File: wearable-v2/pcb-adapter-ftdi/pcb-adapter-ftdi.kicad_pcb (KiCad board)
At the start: 2 copper layers, 27.8 x 19.9 mm, 2 parts, among them J1 FTDI_HERALD, J2 FTDI Pins

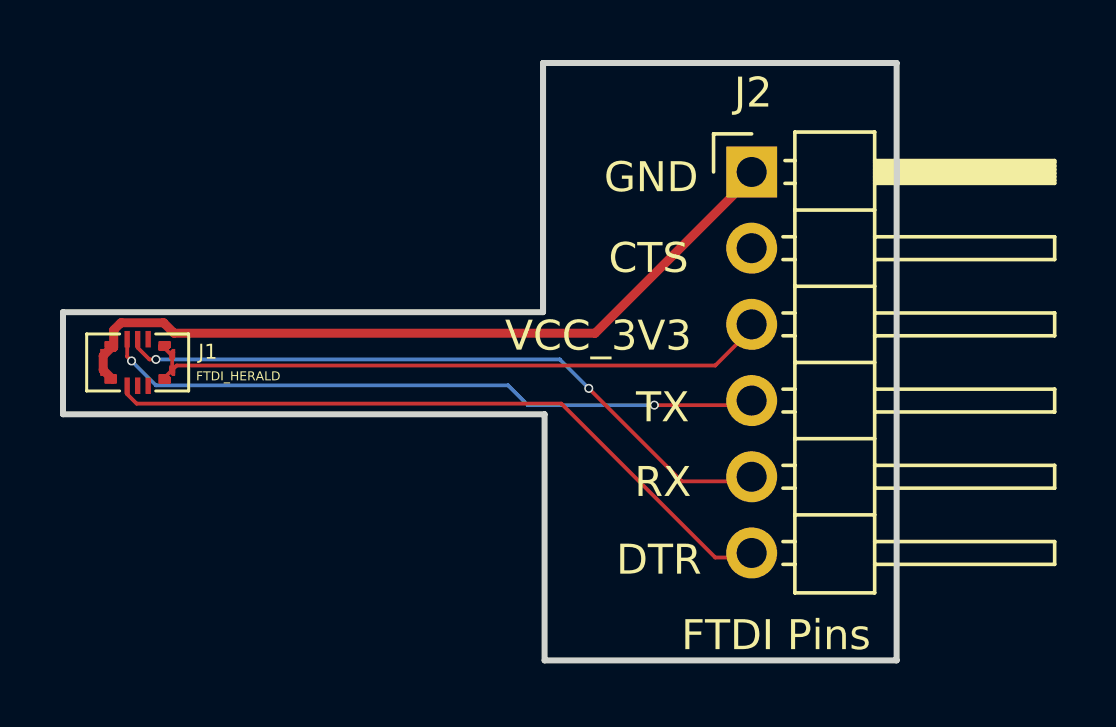
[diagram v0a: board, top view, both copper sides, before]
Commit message: Reworked boards for JLCPCB manufacture
Slightly larger Vias.
Added debug pin holes for Beta testing.
Signed-off-by: Adam Fowler <adam@adamfowler.org>
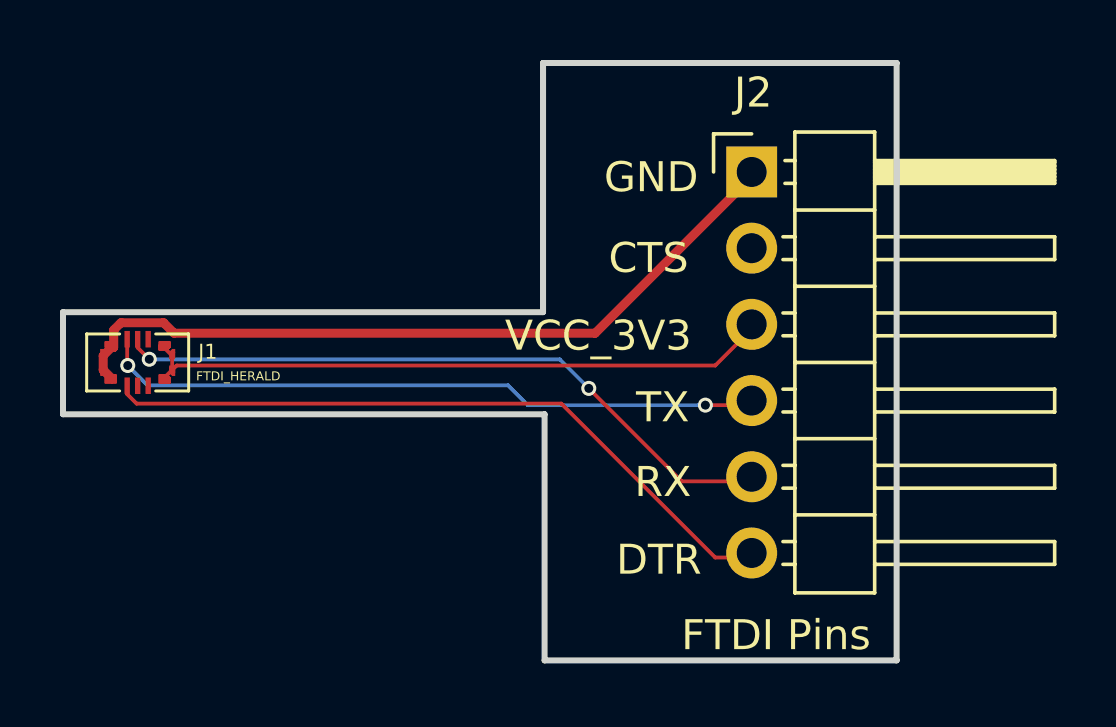
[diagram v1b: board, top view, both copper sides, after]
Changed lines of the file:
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@@
 (kicad_pcb (version 20221018) (generator pcbnew)
   (general
-    (thickness 1.2)
+    (thickness 1.6)
   )
   (paper "A4")
@@
       (layer "F.Mask" (type "Top Solder Mask") (thickness 0.01))
       (layer "F.Cu" (type "copper") (thickness 0.035))
-      (layer "dielectric 1" (type "core") (thickness 1.11) (material "FR4") (epsilon_r 4.5) (loss_tangent 0.02))
+      (layer "dielectric 1" (type "core") (thickness 1.51) (material "FR4") (epsilon_r 4.5) (loss_tangent 0.02))
       (layer "B.Cu" (type "copper") (thickness 0.035))
       (layer "B.Mask" (type "Bottom Solder Mask") (thickness 0.01))
@@
       (svgprecision 4)
       (plotframeref false)
-      (viasonmask false)
+      (viasonmask true)
       (mode 1)
       (useauxorigin true)
@@
         (effects (font (size 0.3 0.3) (thickness 0.075)))
     )
-    (fp_text user "${REFERENCE}" (at 0 0 unlocked) (layer "F.Fab")
+    (fp_text user "${REFERENCE}" (at 2.3622 1.0922 unlocked) (layer "F.Fab")
         (effects (font (size 0.3 0.3) (thickness 0.075)))
     )
@@
         (effects (font (size 1 1) (thickness 0.15)))
     )
-    (fp_text user "${REFERENCE}" (at 2.77 6.35 90) (layer "F.Fab")
+    (fp_text user "${REFERENCE}" (at 2.77 -2.667 180) (layer "F.Fab")
         (effects (font (size 1 1) (thickness 0.15)))
     )
@@
     )
     (stroke (width 0.2) (type solid)) (fill none) (layer "Edge.Cuts"))
-  (gr_text "The Herald Project\nHerald Micro FTDI to 6-pin out\nV1.0 Nov 2023\nLicense: CERN-OHL-P-2" (at 127.8636 84.836 90) (layer "B.SilkS")
+  (gr_text "The Herald Project\nHerald Micro FTDI to 6-pin out\nV1.0 Nov 2023\nLicense: CERN-OHL-P-2" (at 127.9144 84.328 90) (layer "B.SilkS")
     (effects (font (size 0.6 0.6) (thickness 0.15) bold) (justify left bottom mirror))
   )
@@
   (segment (start 125.0286 91.6334) (end 110.99271 91.6334) (width 0.3) (layer "F.Cu") (net 6))
   (segment (start 110.64271 91.2834) (end 109.22489 91.2834) (width 0.3) (layer "F.Cu") (net 6))
-  (segment (start 130.2512 94.0308) (end 127 94.0308) (width 0.127) (layer "F.Cu") (net 7))
-  (segment (start 109.4288 92.4108) (end 109.4288 91.8334) (width 0.127) (layer "F.Cu") (net 7))
-  (segment (start 109.5756 92.5576) (end 109.4288 92.4108) (width 0.127) (layer "F.Cu") (net 7))
-  (via (at 109.5756 92.5576) (size 0.3) (drill 0.2) (layers "F.Cu" "B.Cu") (net 7))
-  (via (at 127 94.0308) (size 0.3) (drill 0.2) (layers "F.Cu" "B.Cu") (net 7))
-  (segment (start 122.1232 93.3704) (end 122.7836 94.0308) (width 0.127) (layer "B.Cu") (net 7))
-  (segment (start 109.5756 92.5576) (end 110.3884 93.3704) (width 0.127) (layer "B.Cu") (net 7))
-  (segment (start 110.3884 93.3704) (end 122.1232 93.3704) (width 0.127) (layer "B.Cu") (net 7))
-  (segment (start 122.7836 94.0308) (end 127 94.0308) (width 0.127) (layer "B.Cu") (net 7))
+  (segment (start 109.4486 92.71) (end 109.4288 92.6902) (width 0.127) (layer "F.Cu") (net 7))
+  (segment (start 130.2512 94.0308) (end 128.7018 94.0308) (width 0.127) (layer "F.Cu") (net 7))
+  (segment (start 109.4288 92.6902) (end 109.4288 91.8334) (width 0.127) (layer "F.Cu") (net 7))
+  (via (at 109.4486 92.71) (size 0.5) (drill 0.3) (layers "F.Cu" "B.Cu") (net 7))
+  (via (at 128.7018 94.0308) (size 0.5) (drill 0.3) (layers "F.Cu" "B.Cu") (net 7))
+  (segment (start 122.7836 94.0308) (end 122.1232 93.3704) (width 0.127) (layer "B.Cu") (net 7))
+  (segment (start 122.1232 93.3704) (end 110.109 93.3704) (width 0.127) (layer "B.Cu") (net 7))
+  (segment (start 128.7018 94.0308) (end 122.7836 94.0308) (width 0.127) (layer "B.Cu") (net 7))
+  (segment (start 110.109 93.3704) (end 109.4486 92.71) (width 0.127) (layer "B.Cu") (net 7))
   (segment (start 109.4288 93.66498) (end 109.4288 93.3834) (width 0.127) (layer "F.Cu") (net 8))
   (segment (start 109.74382 93.98) (end 109.4288 93.66498) (width 0.127) (layer "F.Cu") (net 8))
@@
   (segment (start 123.9012 93.98) (end 109.74382 93.98) (width 0.127) (layer "F.Cu") (net 8))
   (segment (start 130.2512 99.1108) (end 129.032 99.1108) (width 0.127) (layer "F.Cu") (net 8))
-  (segment (start 109.7788 91.8334) (end 109.7788 92.11498) (width 0.127) (layer "F.Cu") (net 9))
+  (segment (start 109.7788 92.11498) (end 109.7788 91.8334) (width 0.127) (layer "F.Cu") (net 9))
   (segment (start 130.2512 96.5708) (end 127.9144 96.5708) (width 0.127) (layer "F.Cu") (net 9))
-  (segment (start 110.17062 92.5068) (end 110.3884 92.5068) (width 0.127) (layer "F.Cu") (net 9))
+  (segment (start 110.16521 92.50139) (end 109.7788 92.11498) (width 0.127) (layer "F.Cu") (net 9))
   (segment (start 127.9144 96.5708) (end 124.8156 93.472) (width 0.127) (layer "F.Cu") (net 9))
-  (segment (start 109.7788 92.11498) (end 110.17062 92.5068) (width 0.127) (layer "F.Cu") (net 9))
-  (via (at 110.3884 92.5068) (size 0.3) (drill 0.2) (layers "F.Cu" "B.Cu") (net 9))
-  (via (at 124.8156 93.472) (size 0.3) (drill 0.2) (layers "F.Cu" "B.Cu") (net 9))
-  (segment (start 124.8156 93.472) (end 123.8504 92.5068) (width 0.127) (layer "B.Cu") (net 9))
-  (segment (start 123.8504 92.5068) (end 110.3884 92.5068) (width 0.127) (layer "B.Cu") (net 9))
+  (via (at 110.16521 92.50139) (size 0.5) (drill 0.3) (layers "F.Cu" "B.Cu") (net 9))
+  (via (at 124.8156 93.472) (size 0.5) (drill 0.3) (layers "F.Cu" "B.Cu") (net 9))
+  (segment (start 110.16521 92.50139) (end 110.17062 92.5068) (width 0.127) (layer "B.Cu") (net 9))
+  (segment (start 110.17062 92.5068) (end 123.8504 92.5068) (width 0.127) (layer "B.Cu") (net 9))
+  (segment (start 123.8504 92.5068) (end 124.8156 93.472) (width 0.127) (layer "B.Cu") (net 9))
 )
